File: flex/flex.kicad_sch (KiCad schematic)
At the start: 131 parts, among them J1 NA_Conn_01x06_Female, J2 NA_Conn_01x05_Female, J3 NA_Conn_01x06_Female, J4 NA_Conn_01x03_Female, J5 NA_Conn_01x03_Female, SW1 SW_Push, SW10 SW_Push, SW11 SW_Push, SW12 SW_Push, SW13 SW_Push, SW14 SW_Push, SW15 SW_Push, SW16 SW_Push, SW17 SW_Push, SW18 SW_Push, SW19 SW_Push, SW2 SW_Push, SW20 SW_Push, SW21 SW_Push, SW22 SW_Push, SW23 SW_Push, SW24 SW_Push, SW3 SW_Push, SW4 SW_Push, SW5 SW_Push, SW6 SW_Push, SW7 SW_Push, SW8 SW_Push, SW9 SW_Push

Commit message: LEDs
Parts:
- added D100, D101, D102, D103, D104, D105, D106, D107, D109, D110, D111, D112, D113, D114, D115, D116, D117, D118, D119, D120, D97, D98, D99: LEFT_LED, libs:SK6812_mini_e_corners_noedgecuts, symbol LED:SK6812MINI
- added D108: RIGHT_LED, libs:SK6812_mini_e_corners_noedgecuts, symbol LED:SK6812MINI
- D13, D14, D15, D16, D17, D18, D19, D20, D21, D22, D23, D24, D37, D38, D39, D40, D41, D42, D43, D44, D45, D46, D47, D48: value SK6812MINI -> RIGHT_LED
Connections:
- net Dout: now also D120.1 (DOUT)
- net Gnd: now also D100.2 (VSS), D101.2 (VSS), D102.2 (VSS), D103.2 (VSS), D104.2 (VSS), D105.2 (VSS), D106.2 (VSS), D107.2 (VSS), D108.2 (VSS), D109.2 (VSS), D110.2 (VSS), D111.2 (VSS), D112.2 (VSS), D113.2 (VSS), D114.2 (VSS), D115.2 (VSS), D116.2 (VSS), D117.2 (VSS), D118.2 (VSS), D119.2 (VSS), D120.2 (VSS), D97.2 (VSS), D98.2 (VSS), D99.2 (VSS)
- net Vcc: now also D100.4 (VDD), D101.4 (VDD), D102.4 (VDD), D103.4 (VDD), D104.4 (VDD), D105.4 (VDD), D106.4 (VDD), D107.4 (VDD), D108.4 (VDD), D97.4 (VDD), D98.4 (VDD), D99.4 (VDD); no longer D37.4 (VDD), D38.4 (VDD), D39.4 (VDD), D40.4 (VDD), D41.4 (VDD), D42.4 (VDD), D43.4 (VDD), D44.4 (VDD), D45.4 (VDD), D46.4 (VDD), D47.4 (VDD), D48.4 (VDD)
- net at D13.3 (DIN), R1.2, R2.2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: now also D37.4 (VDD), D38.4 (VDD), D39.4 (VDD), D40.4 (VDD), D41.4 (VDD), D42.4 (VDD), D43.4 (VDD), D44.4 (VDD), D45.4 (VDD), D46.4 (VDD), D47.4 (VDD), D48.4 (VDD), D109.4 (VDD), D110.4 (VDD), D111.4 (VDD), D112.4 (VDD), D113.4 (VDD), D114.4 (VDD), D115.4 (VDD), D116.4 (VDD), D117.4 (VDD), D118.4 (VDD), D119.4 (VDD), D120.4 (VDD), D97.3 (DIN)
- net at D21.1 (DOUT), D22.3 (DIN): now also D105.1 (DOUT), D106.3 (DIN)
- net at D20.1 (DOUT), D21.3 (DIN): now also D104.1 (DOUT), D105.3 (DIN)
- net at D40.1 (DOUT), D41.3 (DIN): now also D112.1 (DOUT), D113.3 (DIN)
- net at D39.1 (DOUT), D40.3 (DIN): now also D111.1 (DOUT), D112.3 (DIN)
- net at D13.1 (DOUT), D14.3 (DIN): now also D97.1 (DOUT), D98.3 (DIN)
- net at D23.1 (DOUT), D24.3 (DIN): now also D107.1 (DOUT), D108.3 (DIN)
- net at D22.1 (DOUT), D23.3 (DIN): now also D106.1 (DOUT), D107.3 (DIN)
- net at D19.1 (DOUT), D20.3 (DIN): now also D103.1 (DOUT), D104.3 (DIN)
- net at D18.1 (DOUT), D19.3 (DIN): now also D102.1 (DOUT), D103.3 (DIN)
- net at D37.1 (DOUT), D38.3 (DIN): now also D109.1 (DOUT), D110.3 (DIN)
- net at D24.1 (DOUT), D37.3 (DIN): now also D108.1 (DOUT), D109.3 (DIN)
- net at D38.1 (DOUT), D39.3 (DIN): now also D110.1 (DOUT), D111.3 (DIN)
- net at D42.1 (DOUT), D43.3 (DIN): now also D114.1 (DOUT), D115.3 (DIN)
- net at D41.1 (DOUT), D42.3 (DIN): now also D113.1 (DOUT), D114.3 (DIN)
- net at D47.1 (DOUT), D48.3 (DIN): now also D119.1 (DOUT), D120.3 (DIN)
- net at D17.1 (DOUT), D18.3 (DIN): now also D101.1 (DOUT), D102.3 (DIN)
- net at D16.1 (DOUT), D17.3 (DIN): now also D100.1 (DOUT), D101.3 (DIN)
- net at D45.1 (DOUT), D46.3 (DIN): now also D117.1 (DOUT), D118.3 (DIN)
- net at D44.1 (DOUT), D45.3 (DIN): now also D116.1 (DOUT), D117.3 (DIN)
- net at D46.1 (DOUT), D47.3 (DIN): now also D118.1 (DOUT), D119.3 (DIN)
- net at D43.1 (DOUT), D44.3 (DIN): now also D115.1 (DOUT), D116.3 (DIN)
- net at D15.1 (DOUT), D16.3 (DIN): now also D100.3 (DIN), D99.1 (DOUT)
- net at D14.1 (DOUT), D15.3 (DIN): now also D98.1 (DOUT), D99.3 (DIN)
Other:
- moved on the sheet: C1, C2, D37, D38, D39, D40, D41, D42, D43, D44, D45, D46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

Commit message: routing
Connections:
- net Vcc: now also D109.4 (VDD), D110.4 (VDD), D111.4 (VDD), D112.4 (VDD), D113.4 (VDD), D114.4 (VDD), D115.4 (VDD), D116.4 (VDD), D117.4 (VDD), D118.4 (VDD), D119.4 (VDD), D120.4 (VDD), D37.4 (VDD), D38.4 (VDD), D39.4 (VDD), D40.4 (VDD), D41.4 (VDD), D42.4 (VDD), D43.4 (VDD), D44.4 (VDD), D45.4 (VDD), D46.4 (VDD), D47.4 (VDD), D48.4 (VDD)
- new net: D13.3 (DIN), D97.3 (DIN), R1.2, R2.2, R3.2

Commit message: bom
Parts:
- D100, D101, D102, D103, D104, D105, D106, D107, D108, D109, D110, D111, D112, D113, D114, D115, D116, D117, D118, D119, D120, D13, D14, D15, D16, D17, D18, D19, D20, D21, D22, D23, D24, D37, D38, D39, D40, D41, D42, D43, D44, D45, D46, D47, D48, D97, D98, D99: now in the parts list

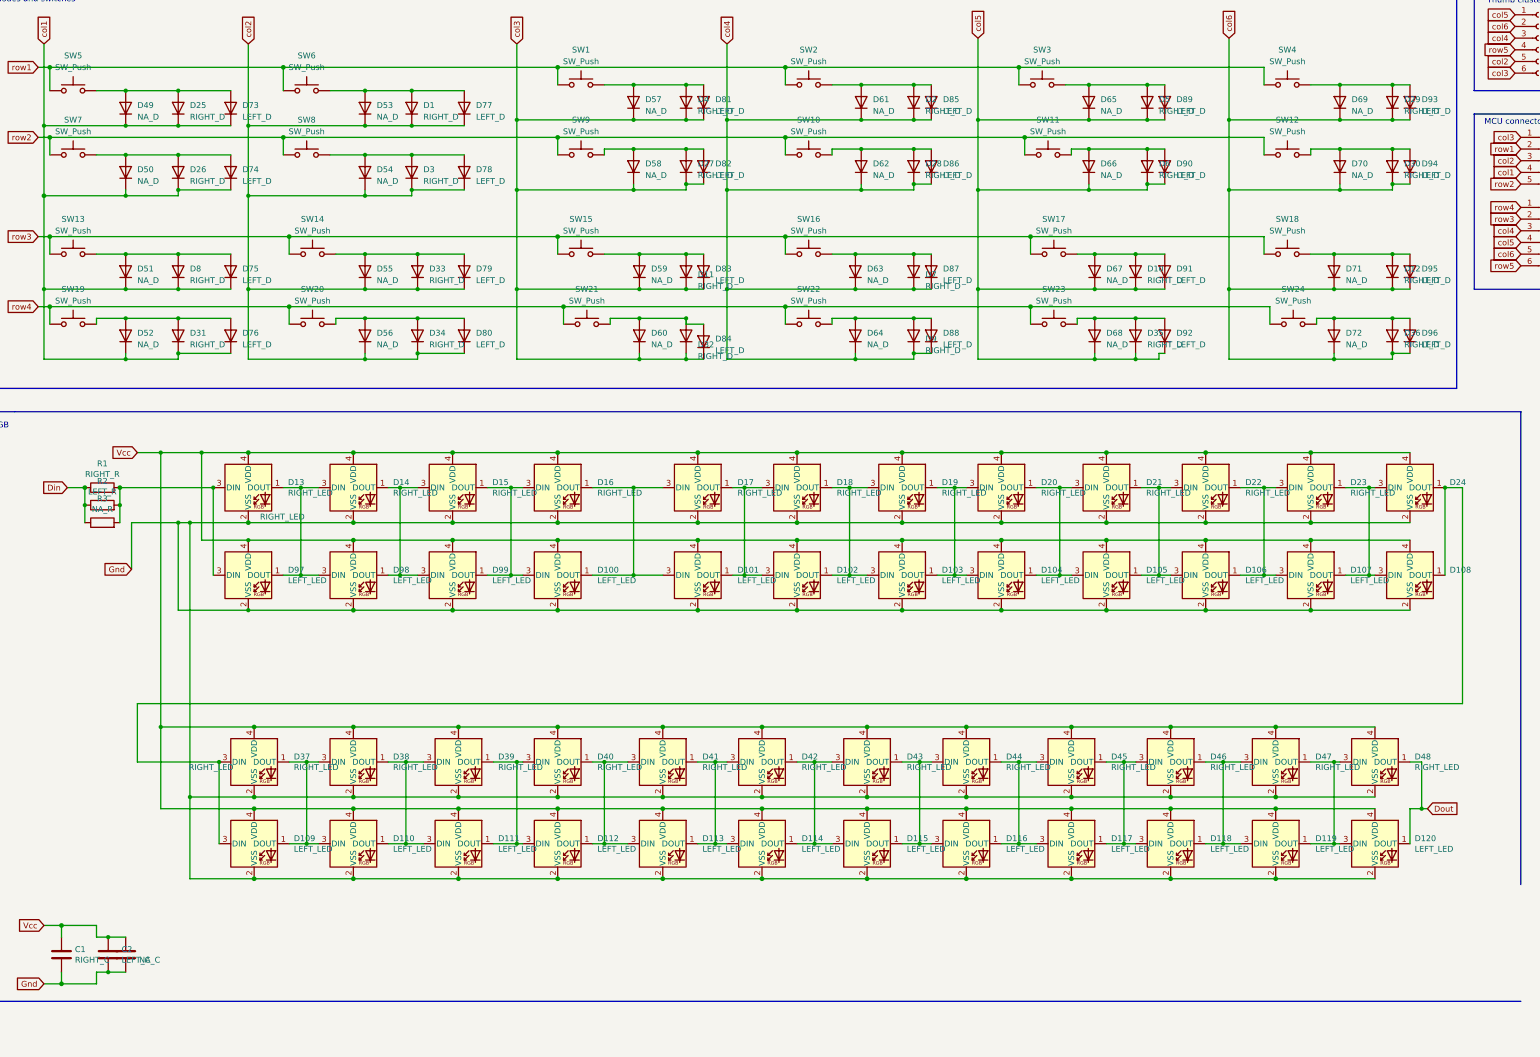
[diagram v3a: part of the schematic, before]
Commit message: remove small diodes
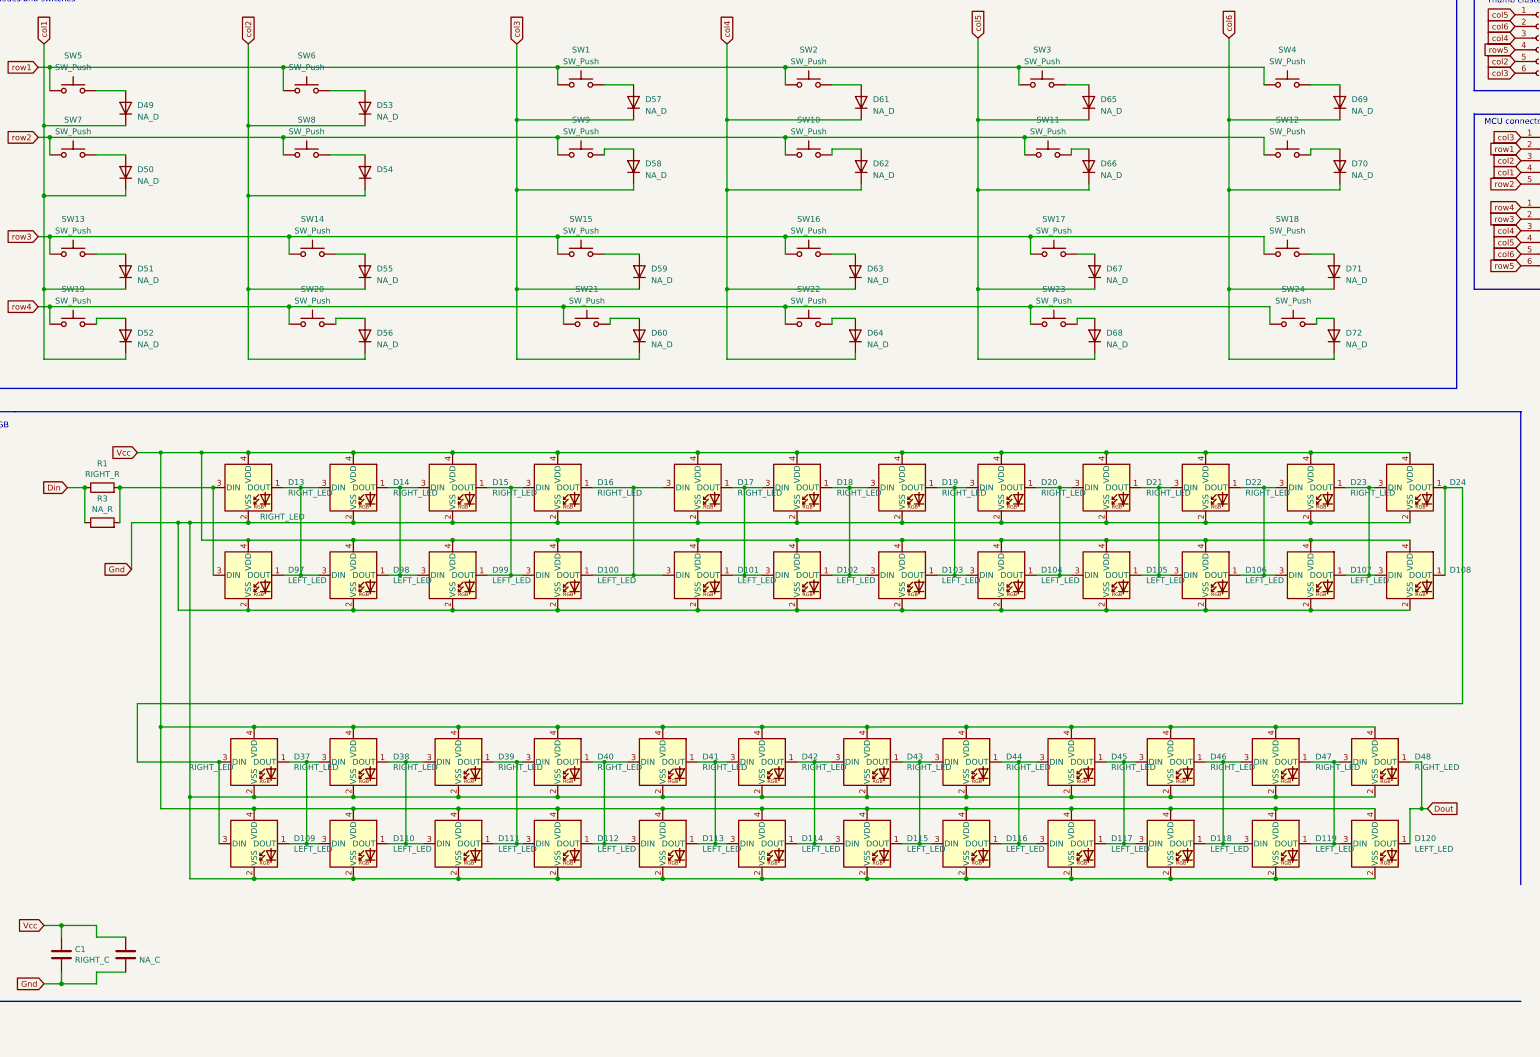
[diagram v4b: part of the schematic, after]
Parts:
- removed C2: LEFT_C, libs:D_0402, symbol Device:C
- removed D1, D10, D11, D12, D2, D25, D26, D27, D28, D29, D3, D30, D31, D32, D33, D34, D35, D36, D4, D5, D6, D7, D8, D9: RIGHT_D, libs:D_SOD-523, symbol Diode:1N4148
- removed D73, D74, D75, D76, D77, D78, D79, D80, D81, D82, D83, D84, D85, D86, D87, D88, D89, D90, D91, D92, D93, D94, D95, D96: LEFT_D, libs:D_SOD-523, symbol Diode:1N4148
- removed R2: LEFT_R, libs:D_0402, symbol Device:R

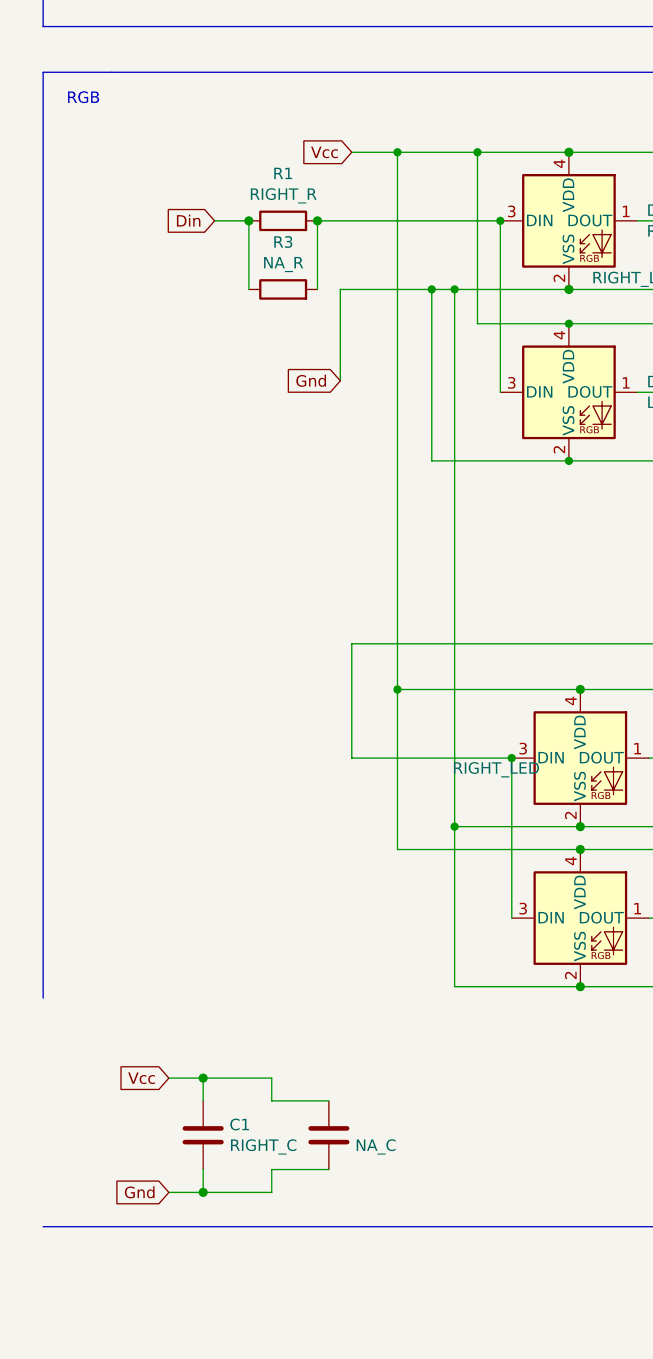
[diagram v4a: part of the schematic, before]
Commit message: solidify main ribbon cable connector
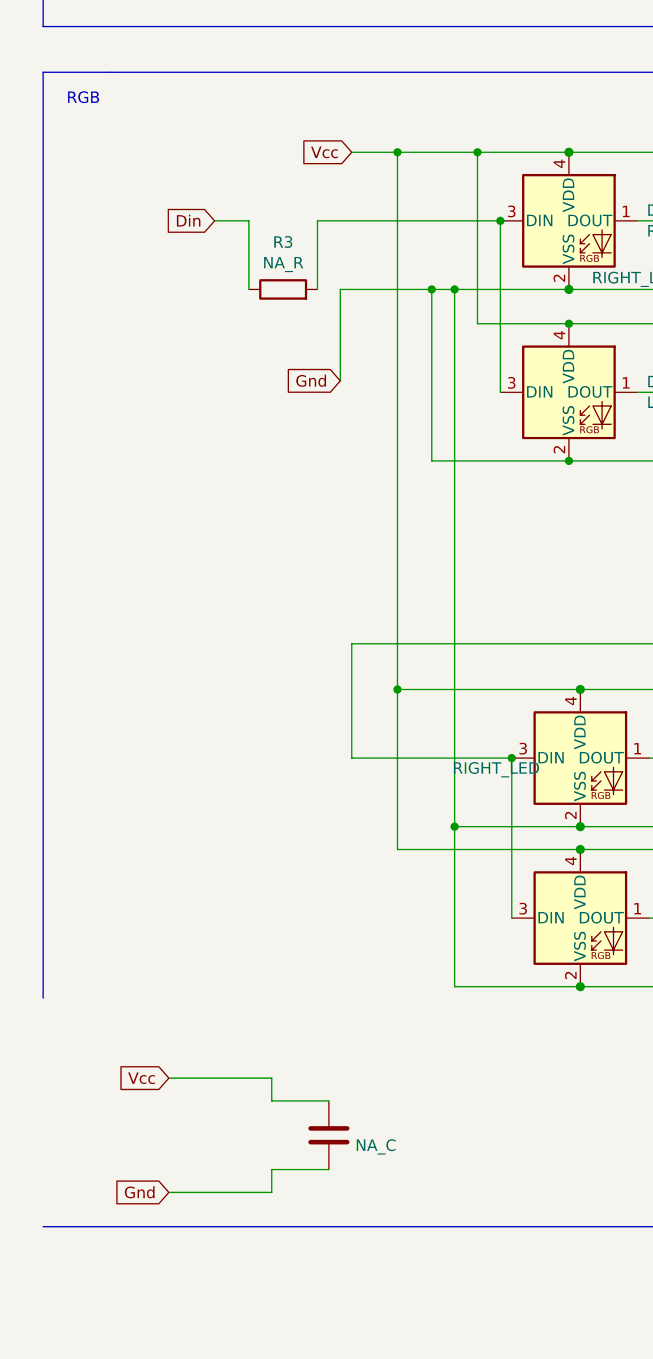
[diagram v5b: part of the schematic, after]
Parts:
- removed C1: RIGHT_C, libs:D_0402, symbol Device:C
- removed R1: RIGHT_R, libs:D_0402, symbol Device:R
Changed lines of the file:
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@@
 	)
 	(junction
-		(at 40.64 222.25)
-		(diameter 1.016)
-		(color 0 0 0 0)
-	)
-	(junction
 		(at 304.8 196.85)
 		(diameter 1.016)
@@
 	)
 	(junction
-		(at 53.34 127)
-		(diameter 1.016)
-		(color 0 0 0 0)
-	)
-	(junction
 		(at 38.1 50.8)
 		(diameter 1.016)
@@
 	)
 	(junction
-		(at 45.72 127)
-		(diameter 1.016)
-		(color 0 0 0 0)
-	)
-	(junction
 		(at 257.81 146.05)
 		(diameter 0)
@@
 	)
 	(junction
-		(at 40.64 234.95)
-		(diameter 1.016)
-		(color 0 0 0 0)
-	)
-	(junction
 		(at 260.35 212.09)
 		(diameter 1.016)
@@
 	(wire
 		(pts
-			(xy 40.64 234.95) (xy 40.64 232.41)
-		)
-		(stroke
-			(width 0)
-			(type solid)
-		)
-	)
-	(wire
-		(pts
 			(xy 234.95 127) (xy 237.49 127)
 		)
@@
 	(wire
 		(pts
-			(xy 40.64 222.25) (xy 36.83 222.25)
-		)
-		(stroke
-			(width 0)
-			(type solid)
-		)
-	)
-	(wire
-		(pts
 			(xy 38.1 87.63) (xy 38.1 91.44)
 		)
@@
 	(wire
 		(pts
-			(xy 36.83 234.95) (xy 40.64 234.95)
+			(xy 36.83 234.95) (xy 48.26 234.95)
 		)
 		(stroke
@@
 	(wire
 		(pts
-			(xy 40.64 224.79) (xy 40.64 222.25)
-		)
-		(stroke
-			(width 0)
-			(type solid)
-		)
-	)
-	(wire
-		(pts
 			(xy 313.69 91.44) (xy 313.69 90.17)
 		)
@@
 	(wire
 		(pts
-			(xy 40.64 234.95) (xy 48.26 234.95)
-		)
-		(stroke
-			(width 0)
-			(type solid)
-		)
-	)
-	(wire
-		(pts
 			(xy 100.33 76.2) (xy 106.68 76.2)
 		)
@@
 	(wire
 		(pts
-			(xy 48.26 222.25) (xy 40.64 222.25)
+			(xy 36.83 222.25) (xy 48.26 222.25)
 		)
 		(stroke
@@
 	)
 	(symbol
-		(lib_id "Device:C")
-		(at 40.64 228.6 0)
-		(unit 1)
-		(exclude_from_sim no)
-		(in_bom yes)
-		(on_board yes)
-		(dnp no)
-		(property "Reference" "C1"
-			(at 43.5611 227.4506 0)
-			(effects
-				(font
-					(size 1.27 1.27)
-				)
-				(justify left)
-			)
-		)
-		(property "Value" "RIGHT_C"
-			(at 43.5611 229.7493 0)
-			(effects
-				(font
-					(size 1.27 1.27)
-				)
-				(justify left)
-			)
-		)
-		(property "Footprint" "libs:D_0402"
-			(at 41.6052 232.41 0)
-			(effects
-				(font
-					(size 1.27 1.27)
-				)
-				(hide yes)
-			)
-		)
-		(property "Datasheet" "~"
-			(at 40.64 228.6 0)
-			(effects
-				(font
-					(size 1.27 1.27)
-				)
-				(hide yes)
-			)
-		)
-		(property "Description" ""
-			(at 40.64 228.6 0)
-			(effects
-				(font
-					(size 1.27 1.27)
-				)
-				(hide yes)
-			)
-		)
-		(pin "1"
-		)
-		(pin "2"
-		)
-		(instances
-			(project "flex"
-				(path "/e63e39d7-6ac0-4ffd-8aa3-1841a4541b55"
-					(reference "C1")
-					(unit 1)
-				)
-			)
-		)
-	)
-	(symbol
 		(lib_id "LED:SK6812MINI")
 		(at 148.59 204.47 0)
@@
 					(unit 1)
 				)
-			)
-		)
-	)
-	(symbol
-		(lib_id "Device:R")
-		(at 49.53 127 90)
-		(unit 1)
-		(exclude_from_sim no)
-		(in_bom yes)
-		(on_board yes)
-		(dnp no)
-		(property "Reference" "R1"
-			(at 49.53 121.7738 90)
-			(effects
-				(font
-					(size 1.27 1.27)
-				)
-			)
-		)
-		(property "Value" "RIGHT_R"
-			(at 49.53 124.0725 90)
-			(effects
-				(font
-					(size 1.27 1.27)
-				)
-			)
-		)
-		(property "Footprint" "libs:D_0402"
-			(at 49.53 128.778 90)
-			(effects
-				(font
-					(size 1.27 1.27)
-				)
-				(hide yes)
-			)
-		)
-		(property "Datasheet" "~"
-			(at 49.53 127 0)
-			(effects
-				(font
-					(size 1.27 1.27)
-				)
-				(hide yes)
-			)
-		)
-		(property "Description" ""
-			(at 49.53 127 0)
-			(effects
-				(font
-					(size 1.27 1.27)
-				)
-				(hide yes)
-			)
-		)
-		(pin "1"
-		)
-		(pin "2"
-		)
-		(instances
-			(project "flex"
-				(path "/e63e39d7-6ac0-4ffd-8aa3-1841a4541b55"
-					(reference "R1")
-					(unit 1)
-				)
